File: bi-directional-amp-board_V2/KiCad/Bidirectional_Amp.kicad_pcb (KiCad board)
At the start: 4 copper layers, 52 x 68.4 mm, 135 parts, among them J1 142-0701-851_ALT, J2 142-0701-851_ALT, J3 142-0701-851_ALT, J4 142-0701-851_ALT, J6 142-0701-851_ALT, J7 142-0701-851_ALT, SW1 TL36PO, U1 SN74LVC1G32DBVR, U10 TQP9111, U11 SN74LV1T34DBVR, U12 SN74LVC1G32DBVR, U2 LTC6994-1, U3 LTC6994-1, U4 TQP3M9037, U5 TQP3M9037, U6 SN74LV1T34DBVR, U7 QPC1022, U8 QPC1022, U9 SN74LV1T34DBVR

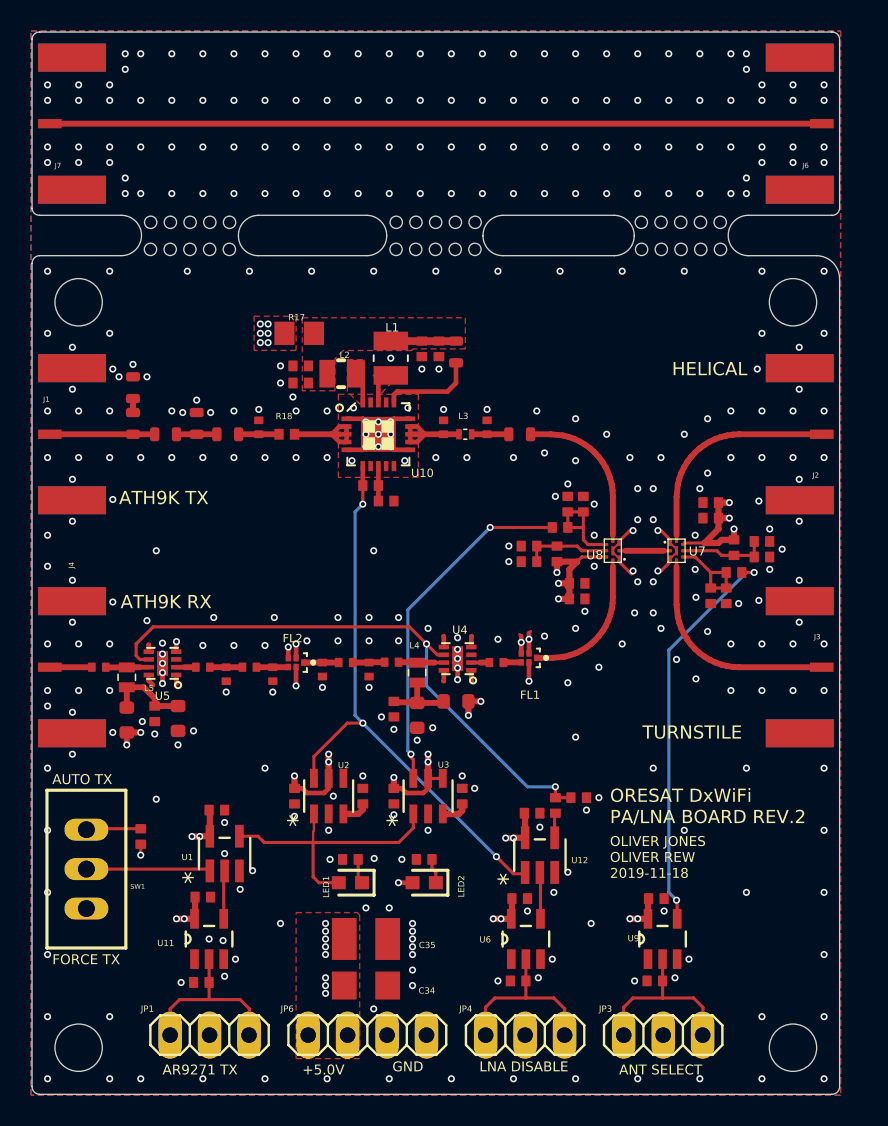
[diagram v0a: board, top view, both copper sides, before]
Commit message: Updated KiCAD import of bidirectional amplifier. Still a bit broken, but better now.
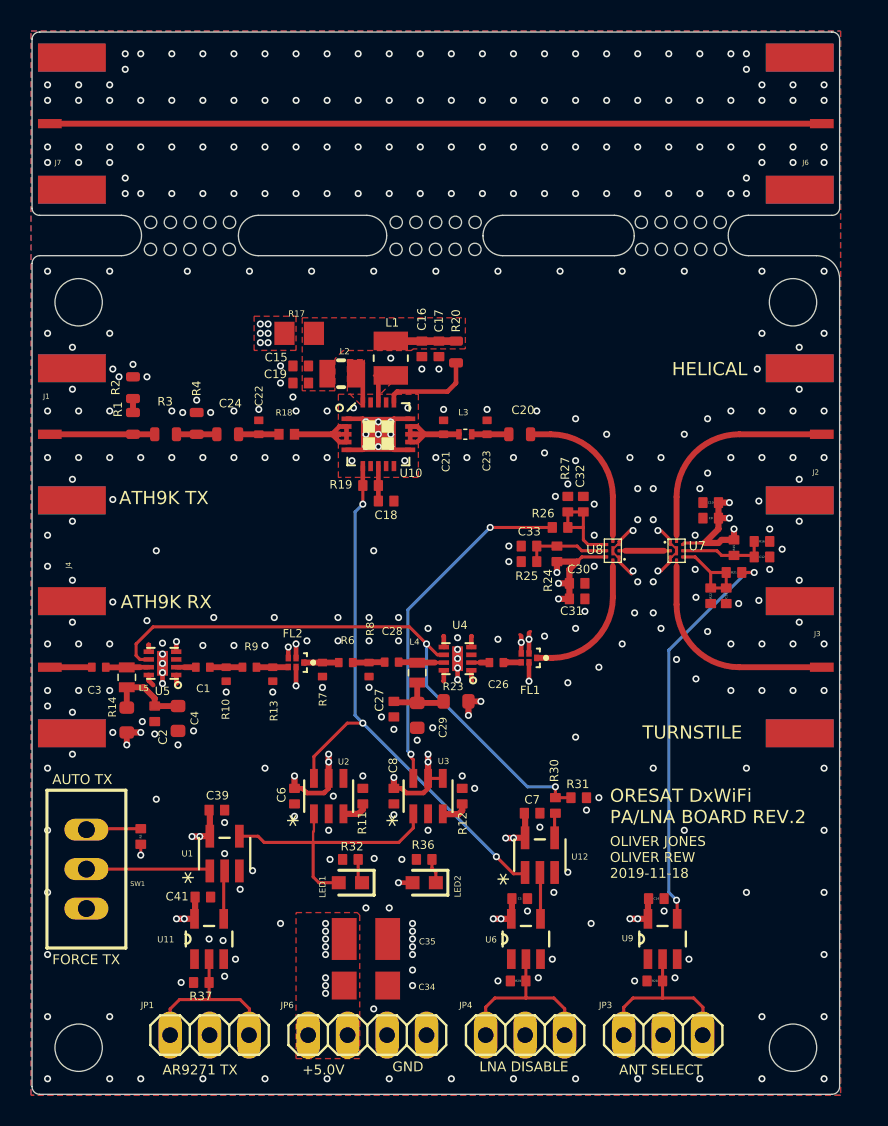
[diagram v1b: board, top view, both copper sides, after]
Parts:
- C34: footprint Bidirectional_Amp:C1206 -> Bidirectional_Amp:C1206_334
- C35: footprint Bidirectional_Amp:C1210 -> Bidirectional_Amp:C1210_334
- JP1, JP3, JP4: footprint Bidirectional_Amp:1X03 -> Bidirectional_Amp:1X03_325
- JP6: footprint Bidirectional_Amp:1X04 -> Bidirectional_Amp:1X04_325
- R17: footprint Bidirectional_Amp:R0805 -> Bidirectional_Amp:R0805_334
- R18: footprint Bidirectional_Amp:R0402 -> Bidirectional_Amp:R0402_334
- SW1: footprint Bidirectional_Amp:TL3XPO -> Bidirectional_Amp:TL3XPO_380
